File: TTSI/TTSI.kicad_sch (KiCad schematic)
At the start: 33 parts, among them Q101 NMOS, Q102 NMOS, Q103 NMOS, Q104 PMOS, Q105 NMOS, Q106 NMOS, U101 641964-1, U102 641964-1, U103 R-78E5.0-0.5, U104 74AHC1G32, U105 641964-1, U106 74AHC1G08, U107 LM555xM, U108 641964-1

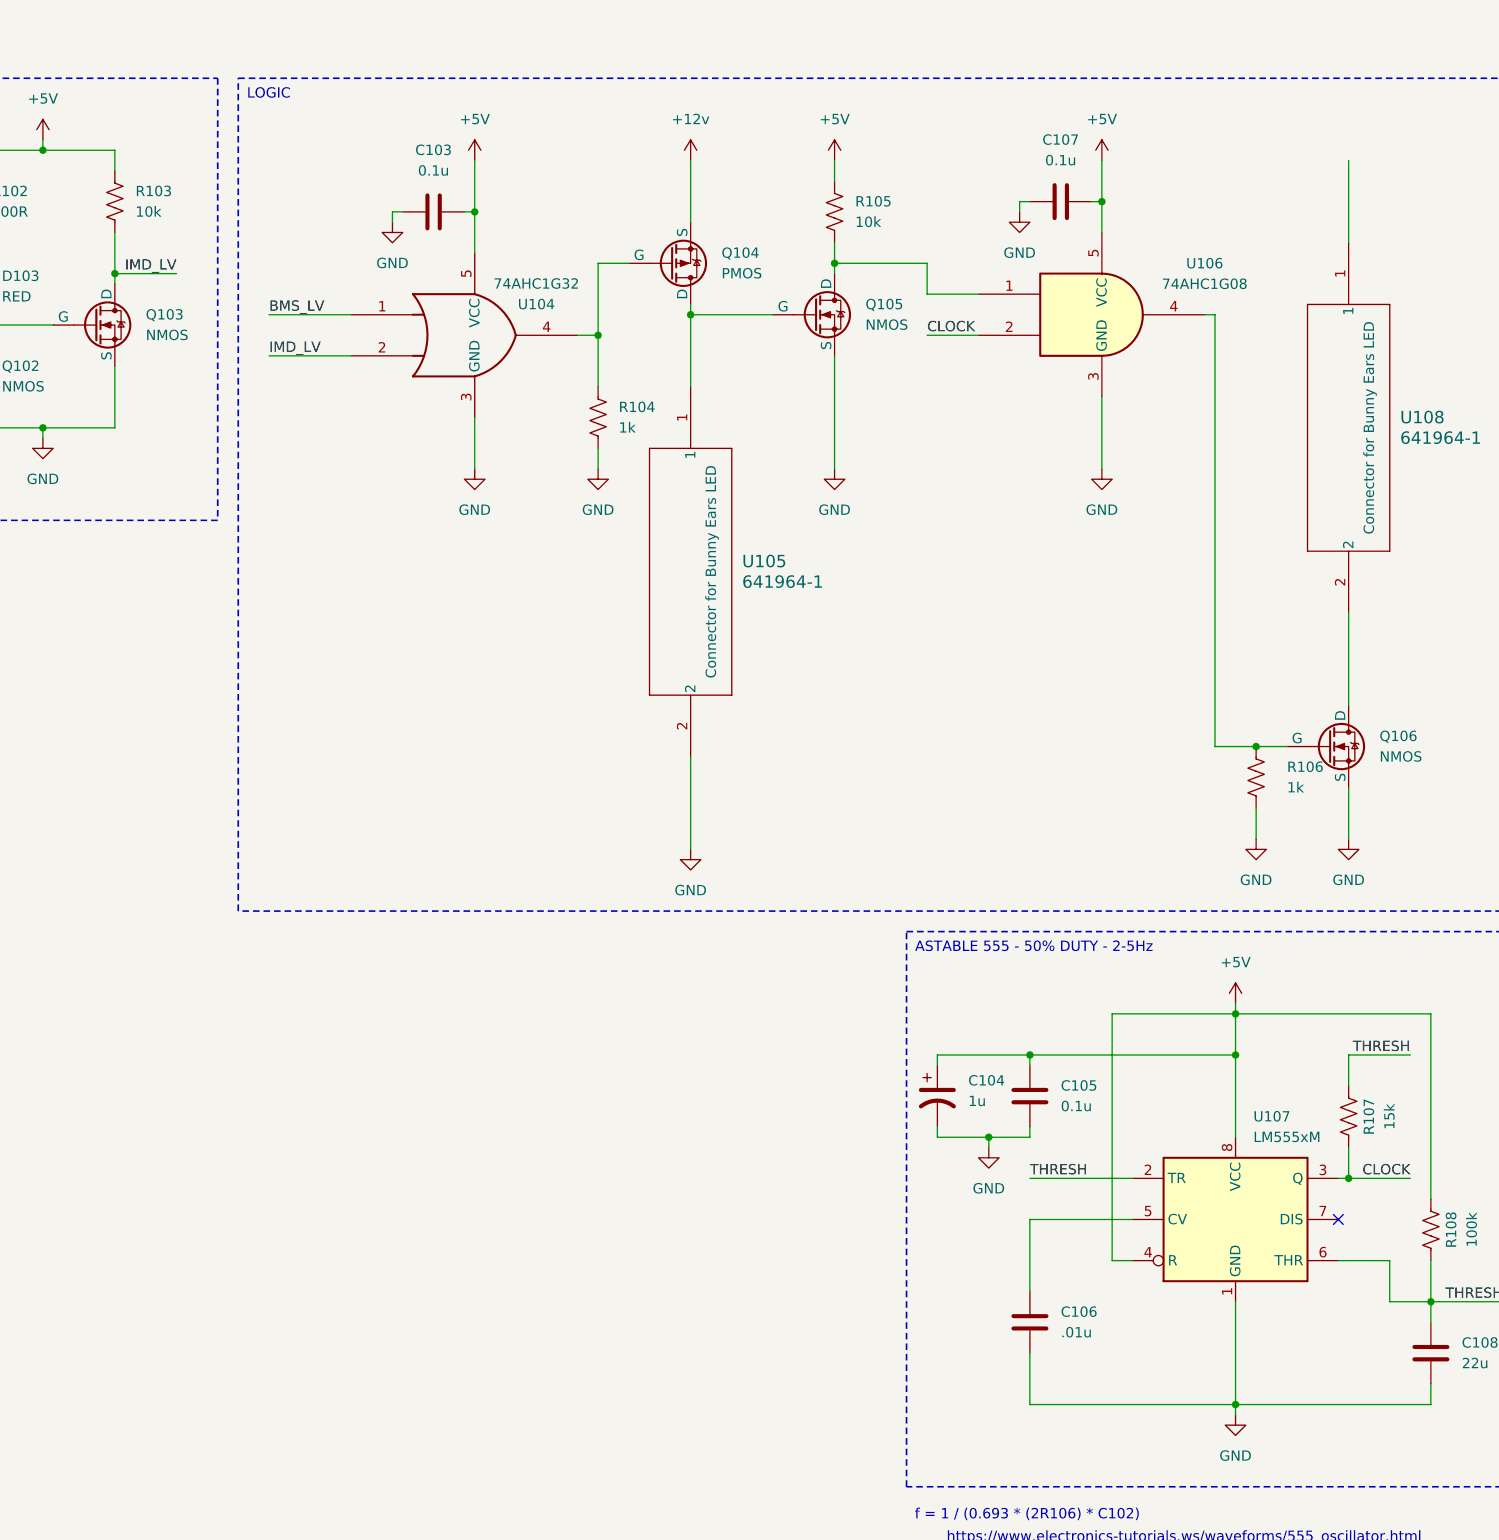
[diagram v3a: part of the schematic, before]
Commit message: Layout, routing, footprint addition, constraints set. Some component nets might be too small idk. But needs revision
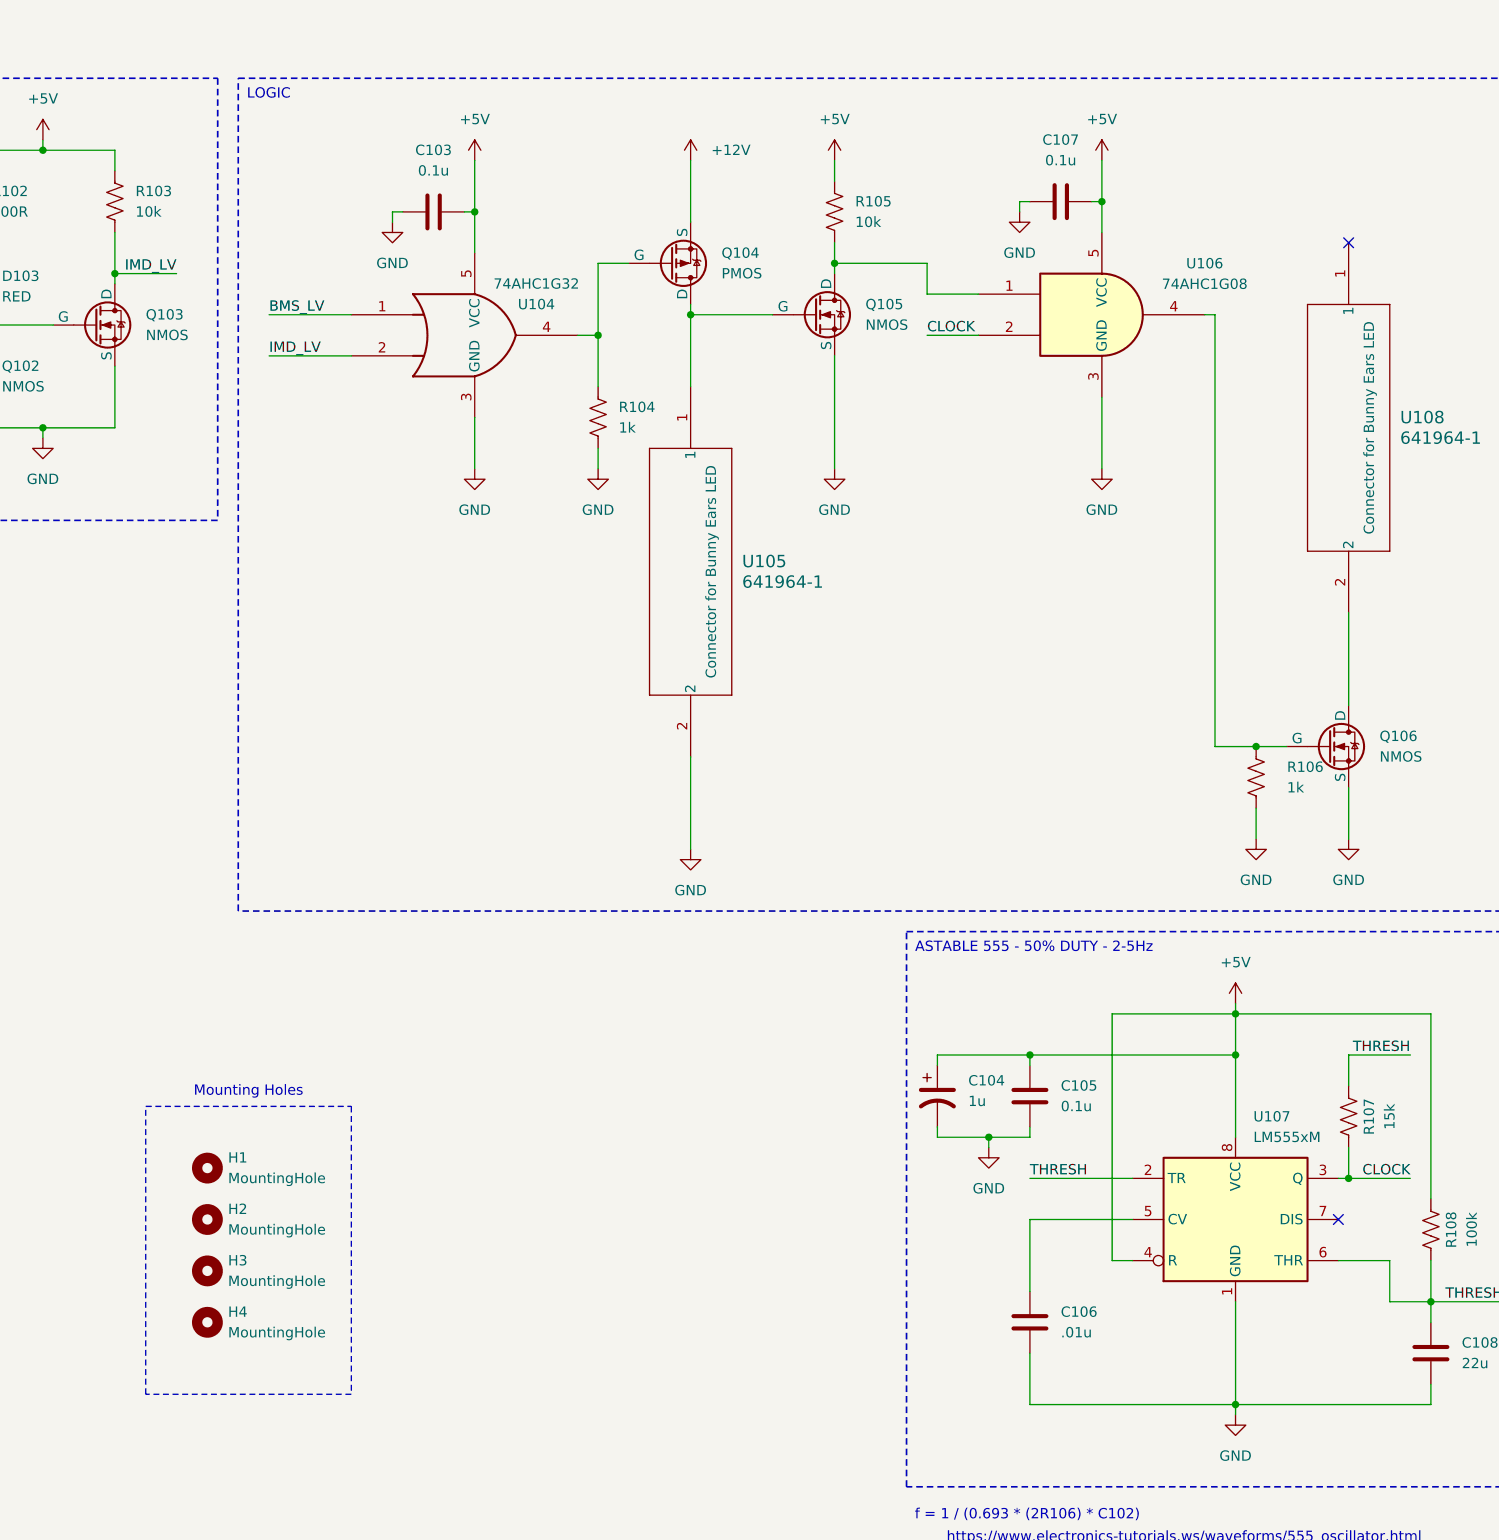
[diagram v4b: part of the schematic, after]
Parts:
- added H1, H2, H3, H4: MountingHole, MountingHole:MountingHole_2.2mm_M2, symbol Mechanical:MountingHole
- U101, U102: footprint (none) -> 641964-1:641964-1_TYC; symbol CONNECTOR:641964-1 -> 641964-1:641964-1
- U103: footprint Converter_DCDC:Converter_DCDC_RECOM_R-78E-0.5_THT -> R_78E5_0_0_5 (1):R-78E-0.5_RCP
- U105, U108: footprint (none) -> 641964-1:641964-1_TYC
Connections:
- net +12v is gone; now on net +12V: Q104.3 (S)
- no-connect marks 1 -> 2
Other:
- note added: "Mounting Holes"

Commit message: Changes to RML and TSSI
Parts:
- removed U108: 641964-1, 641964-1:641964-1_TYC, symbol CONNECTOR:641964-1
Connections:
- net GND: no longer U105.2
- net at Q106.1 (D): now also U105.2
- no-connect marks 2 -> 1
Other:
- moved on the sheet: C101, C102
